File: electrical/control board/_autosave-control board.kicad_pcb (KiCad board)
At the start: 4 copper layers, 72.4 x 149.8 mm, 57 parts, among them J1 analog_extra, J10 Motor_2, J11 Motor_3, J12 Motor_4, J13 Motor_5, J14 Motor_6, J15 Motor_7, J16 Motor_8, J2 Programming_Header, J3 Conn_01x08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

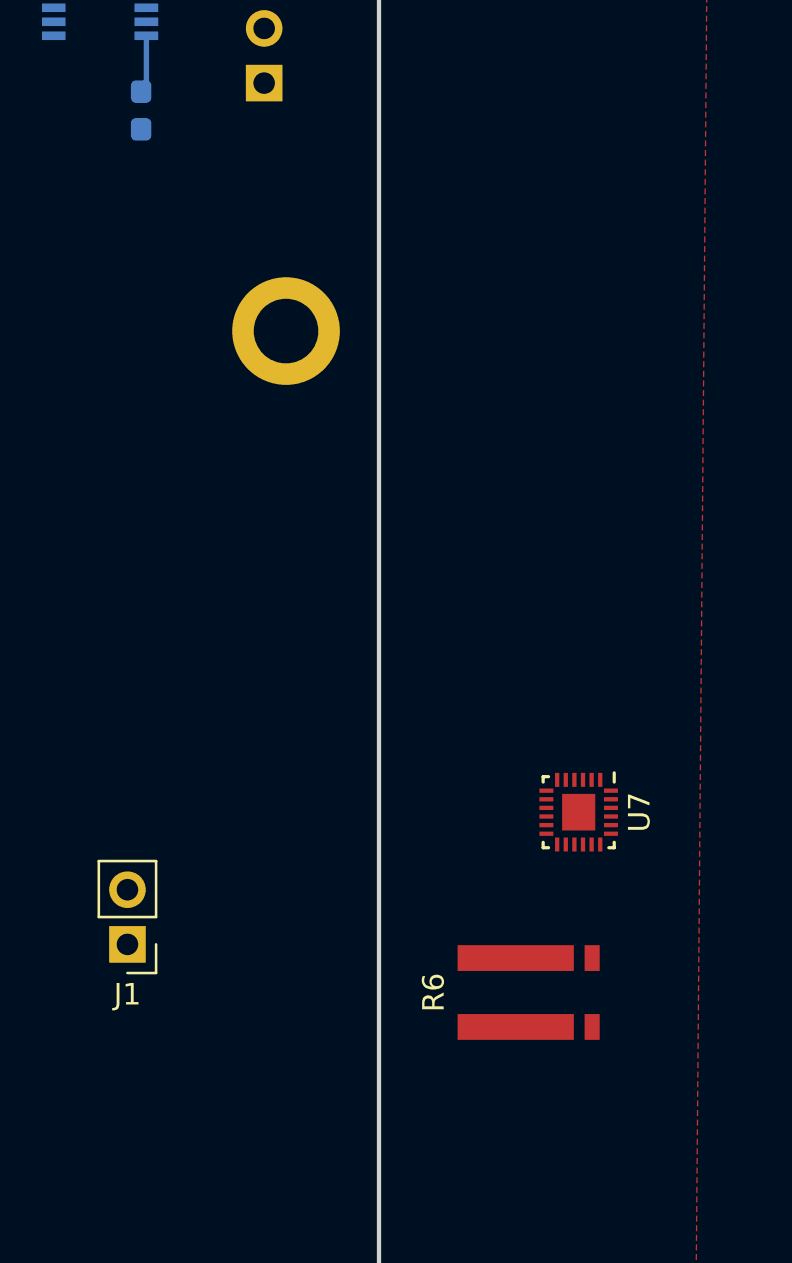
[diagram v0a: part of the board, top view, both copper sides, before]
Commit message: Moved current measurement to power board
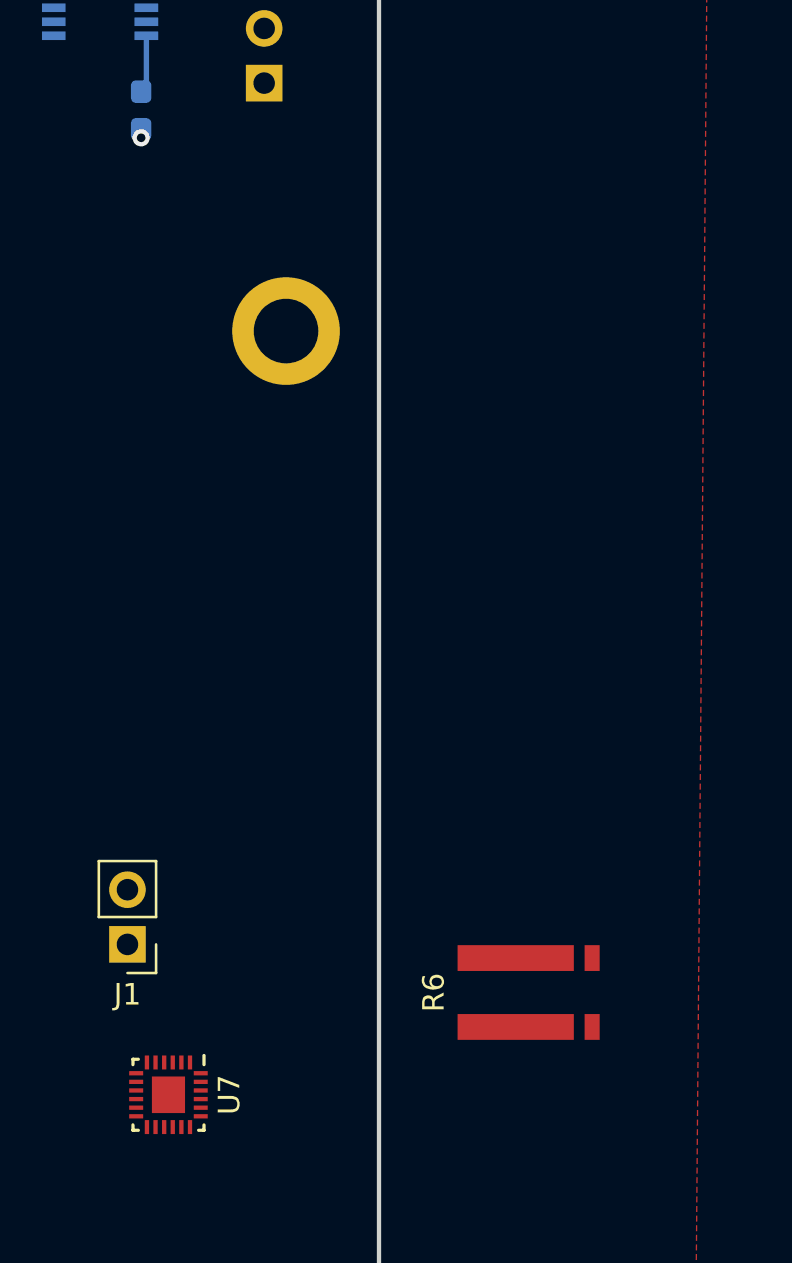
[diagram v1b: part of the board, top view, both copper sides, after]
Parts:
- moved U7 23.1 mm to (93.3, 149.9)
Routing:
- net GND: vias 6 -> 7
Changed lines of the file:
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@@
     (thickness 1.6)
     (drawings 2)
-    (tracks 38)
+    (tracks 39)
     (zones 0)
     (modules 57)
@@
   )
   (module footprints:ICM-20648 (layer F.Cu)
-    (at 112.399 136.735 270)
+    (at 93.345 149.86 270)
     (attr smd)
     (fp_text reference U7 (at 0 -2.825 270) (layer F.SilkS)
@@
   (gr_arc (start 105.664 94.190937) (end 103.124 19.304) (angle -176.1147961) (layer Edge.Cuts) (width 0.2))
   (gr_line (start 103.124 19.304) (end 103.124 169.077874) (layer Edge.Cuts) (width 0.2))
+  (via (at 92.075 105.41) (size 0.8) (drill 0.4) (layers F.Cu B.Cu) (net 1))
   (via (at 67.31 90.17) (size 0.8) (drill 0.4) (layers F.Cu B.Cu) (net 1))
   (via (at 73.66 90.17) (size 0.8) (drill 0.4) (layers F.Cu B.Cu) (net 1))
